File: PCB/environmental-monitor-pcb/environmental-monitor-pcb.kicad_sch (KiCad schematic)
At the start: 4 parts, among them J2 ESP32 RIGHT HEADER, J3 BME280 MODULE, J4 SSD1306 OLED

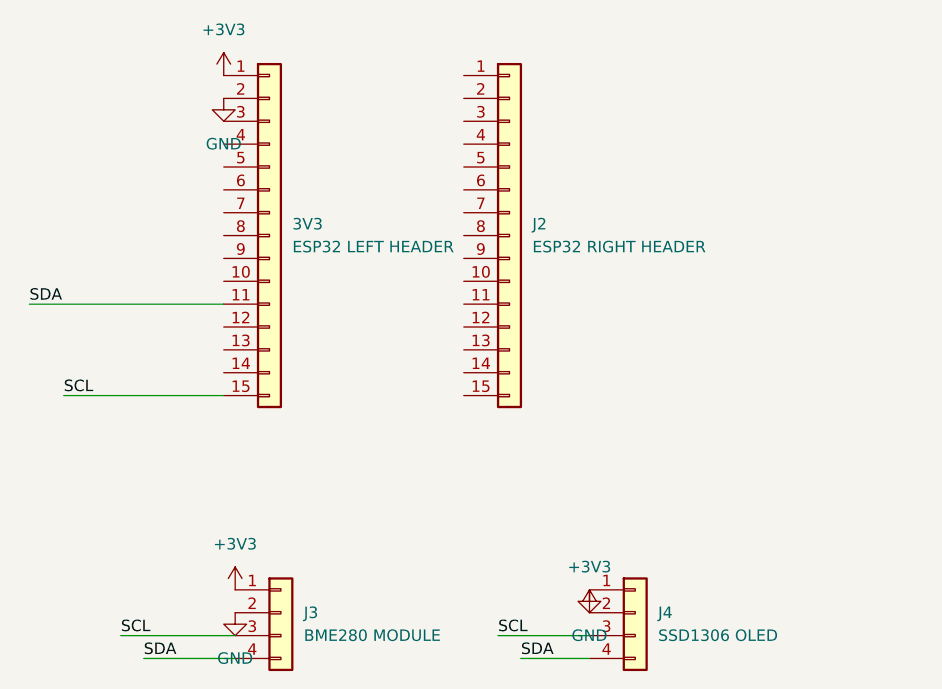
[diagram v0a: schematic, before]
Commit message: Add microSD card to environmental monitor PCB
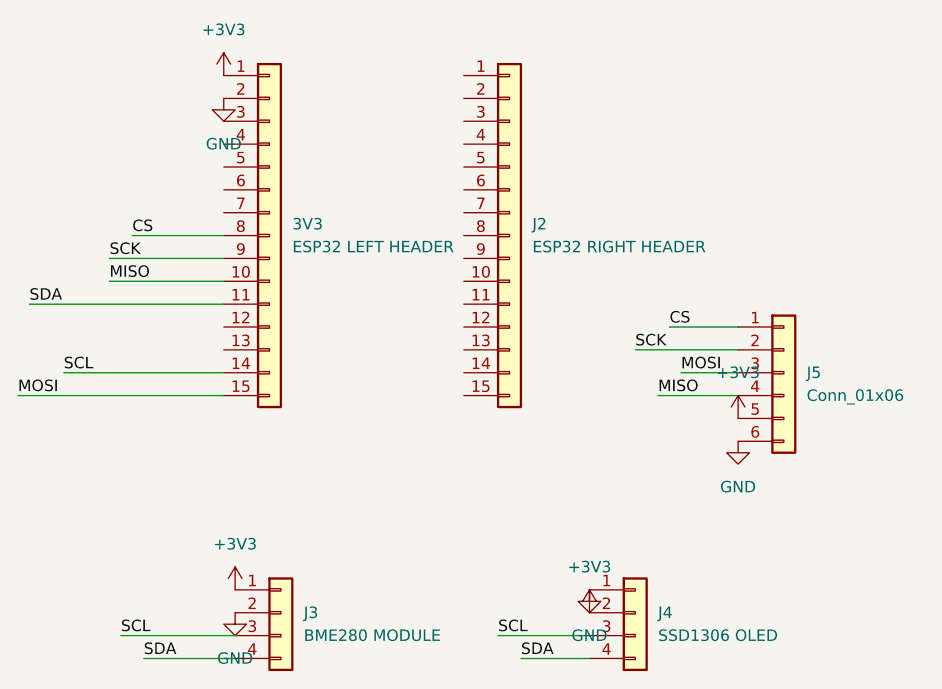
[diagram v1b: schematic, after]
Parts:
- added J5: Conn_01x06, Connector_PinHeader_2.54mm:PinHeader_1x06_P2.54mm_Vertical, symbol Connector_Generic:Conn_01x06
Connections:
- net +3V3: now also J5.5 (Pin_5)
- net GND: now also J5.6 (Pin_6)
- net SCL: now also 3V3.14 (Pin_14); no longer 3V3.15 (Pin_15)
- net MISO: now reaches 3V3.10 (Pin_10)
- net MISO: now also J5.4 (Pin_4)
- net CS: now reaches 3V3.8 (Pin_8)
- net CS: now also J5.1 (Pin_1)
- net SCK: now reaches 3V3.9 (Pin_9)
- net SCK: now also J5.2 (Pin_2)
- new net MOSI: 3V3.15 (Pin_15), J5.3 (Pin_3)
